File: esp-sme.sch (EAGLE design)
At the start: 30 parts, among them J2 BME280, J3 UART, Q1 MOSFET-NCH-AO3404A, Q2 MOSFET-NCH-AO3404A, Q3 NPN, Q4 NPN, Q5 NPN, U2 MIC5504

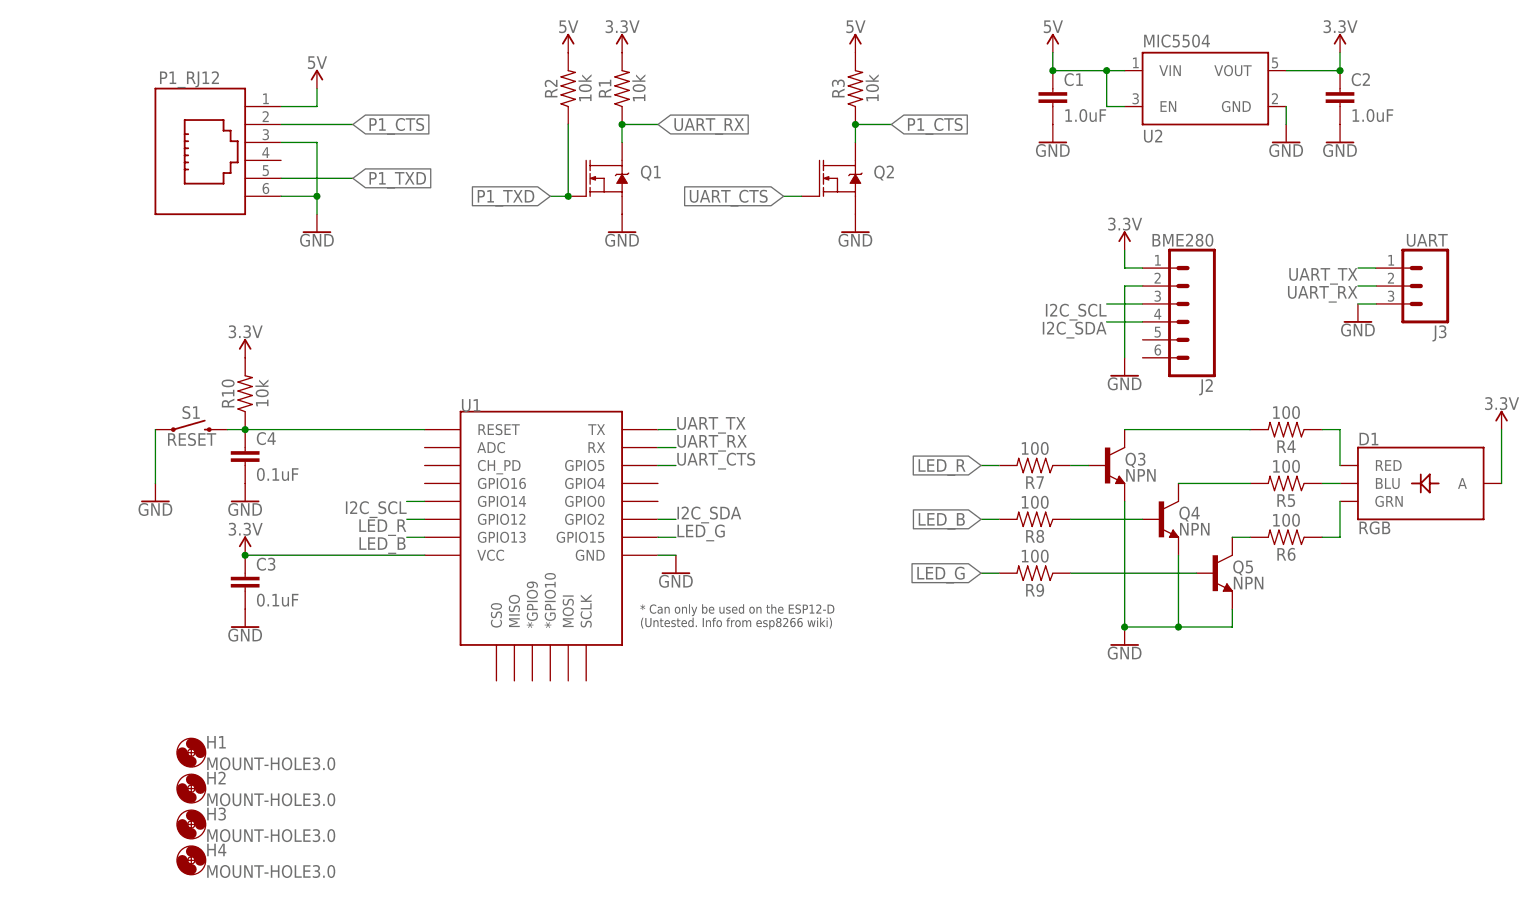
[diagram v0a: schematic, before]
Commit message: Added boot-pin configuration
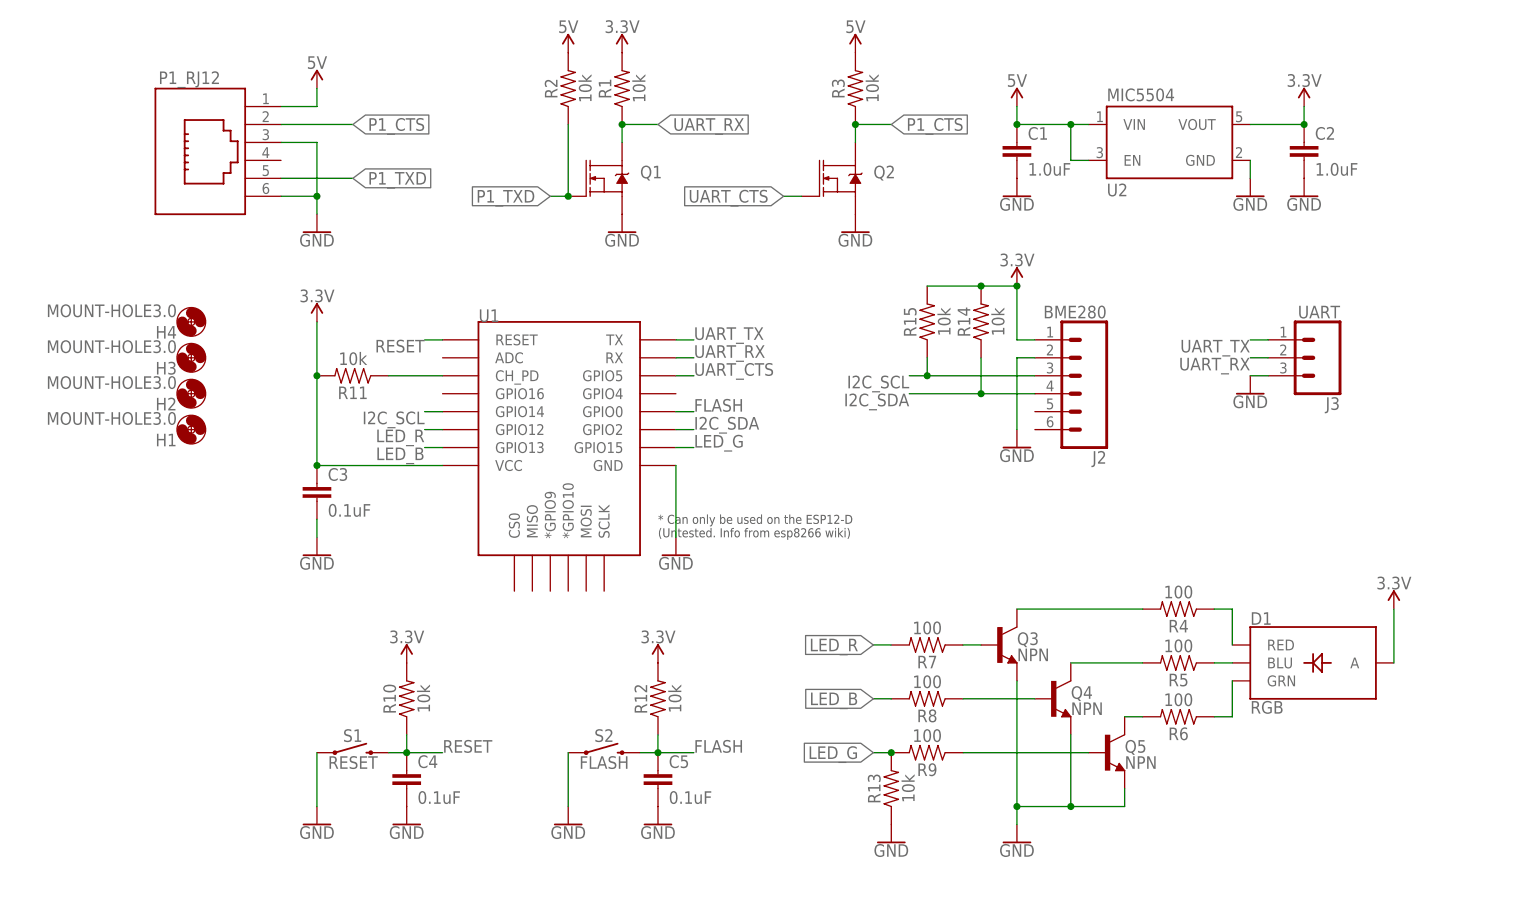
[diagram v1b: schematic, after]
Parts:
- added C5: 0.1uF, SparkFun-Capacitors:0.1UF-0603-25V-5%
- added R11, R12, R13, R14, R15: 10k, SparkFun-Resistors:10KOHM-0603-1/10W-1%
- added S2: FLASH, SparkFun-Switches:MOMENTARY-SWITCH-SPST-SMD-4.6X2.8MM
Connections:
- net N$10 renamed RESET
- new net FLASH: C5.1, R12.1, S2.2, U1.GPIO0
- new net N$11: R11.1, U1.CH_PD
- net 3.3V: now also R11.2, R12.2, R14.2, R15.2
- net GND: now also C5.2, R13.1, S2.1
- net I2C_SCL: now also R15.1
- net I2C_SDA: now also R14.1
- net LED_G: now also R13.2
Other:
- moved on the sheet: C1, C2, C3, C4, D1, H1, H2, H3, H4, J2, J3, Q3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
